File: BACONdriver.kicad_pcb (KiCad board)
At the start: 2 copper layers, 20 parts, among them P1 Batt_Mon, P10 Motor_Ctrl, P11 Batt, P4 Stearing, P5 D8, P6 V_Sel, P7 A5, P8 Batt_Current, P9 FTDI, U1 LM358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

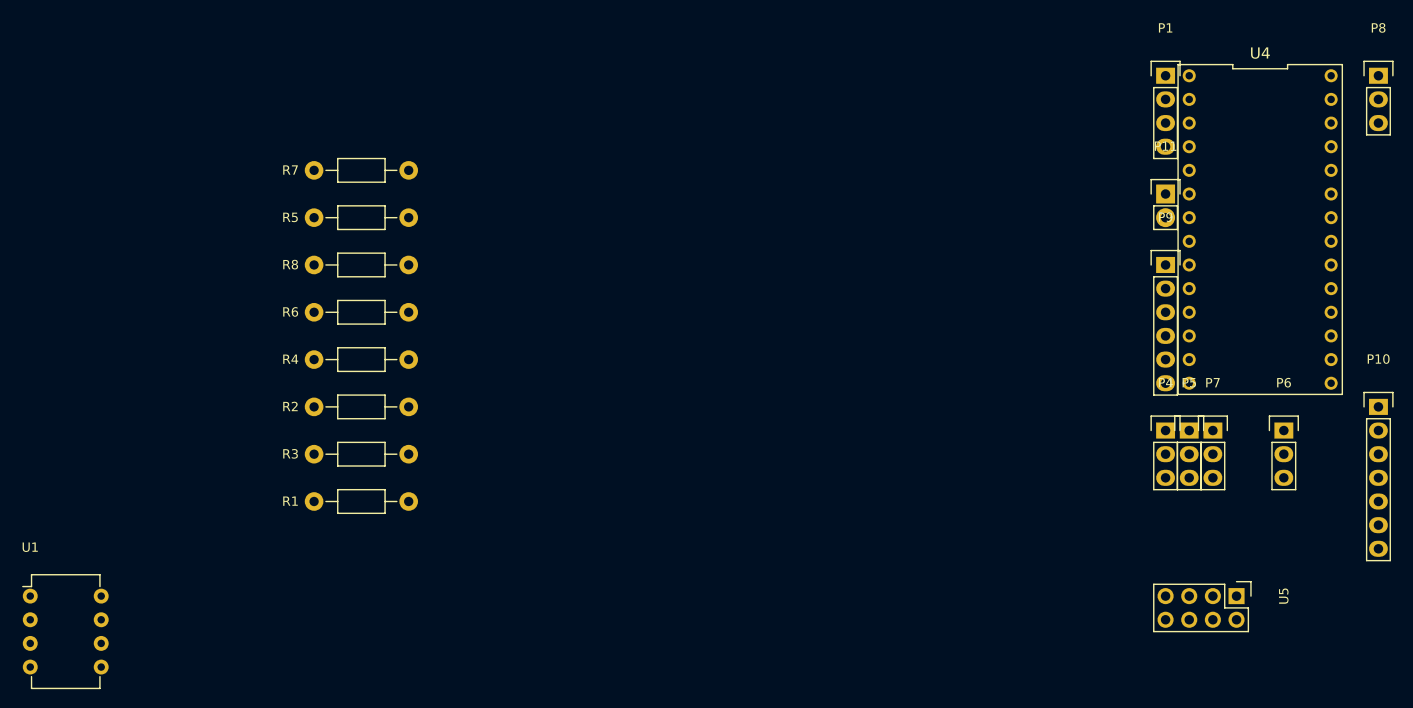
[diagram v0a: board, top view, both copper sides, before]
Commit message: Modified to use a simple voltage divider for battery voltage measurement, the op amp version would not fit on the prototype board and not really needed. Also added headers to allow the FTDI TX/RX to be swapped.
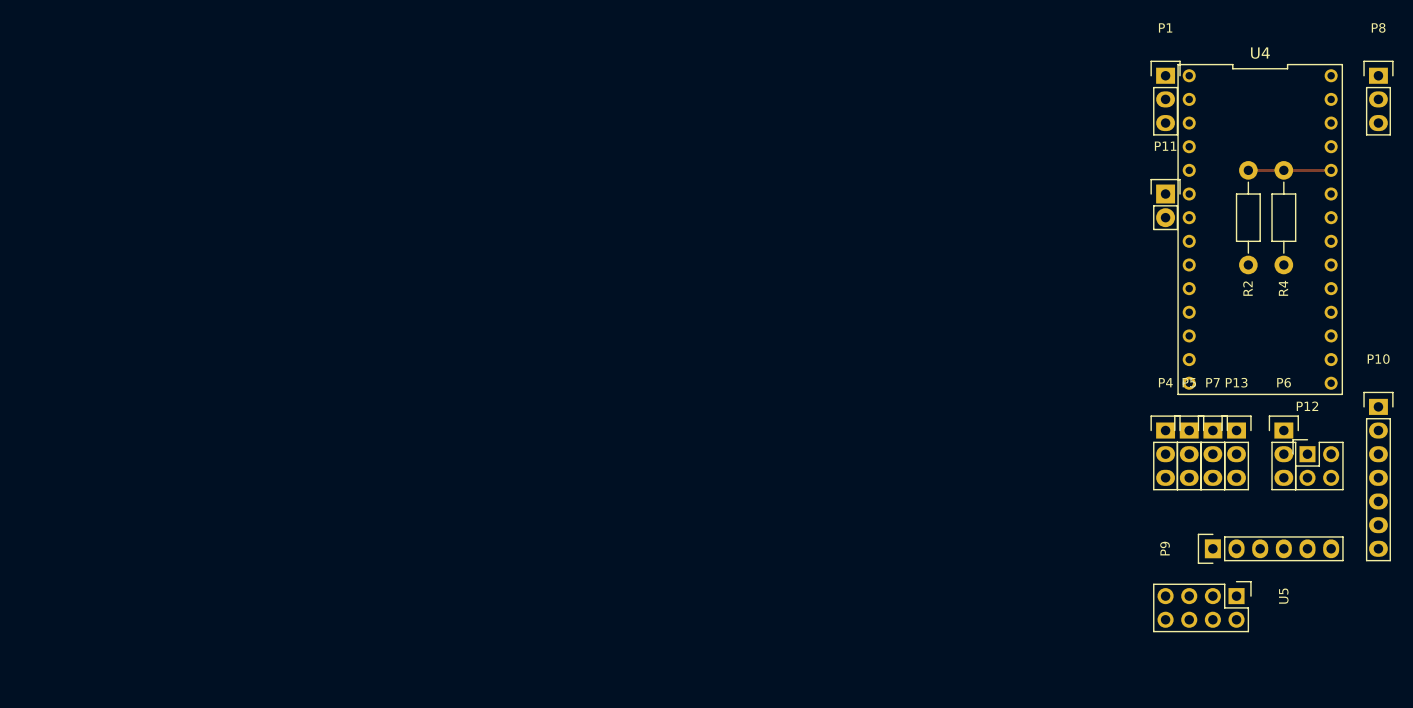
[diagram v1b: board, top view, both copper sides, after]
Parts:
- removed R1, R3, R5, R6, R7, R8: 10K, Resistors_ThroughHole:Resistor_Horizontal_RM10mm
- removed U1: LM358, Housings_DIP:DIP-8_W7.62mm
- added P12: Cross, Pin_Headers:Pin_Header_Straight_2x02, F.Cu at (172.7, 109.2)
- added P13: A5, Pin_Headers:Pin_Header_Straight_1x03, F.Cu at (165.1, 106.7)
- P1: footprint Pin_Headers:Pin_Header_Straight_1x04 -> Pin_Headers:Pin_Header_Straight_1x03
- P7: value A5 -> A4
- moved R4 104.6 mm to (170.2, 88.9), turned to 90 degrees
- moved R2 93.7 mm to (166.4, 78.7), turned to 270 degrees
- moved P9 30.9 mm to (162.6, 119.4), turned to 90 degrees
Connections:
- P7 pad 3: /Control_Board/A5 -> /Control_Board/A4
- P9 pad 4: /Control_Board/TXD -> Net-(P12-Pad3)
- P9 pad 5: /Control_Board/RXD -> Net-(P12-Pad2)
- R2 pad 1: Net-(R2-Pad1) -> /Control_Board/A1
- R2 pad 2: /Control_Board/A0 -> /Control_Board/Cell2
- R4 pad 2: Net-(R2-Pad1) -> /Control_Board/A1
- U4 pad 10: (no net) -> /Control_Board/A1
- U4 pad 4: (no net) -> /Control_Board/A4
- U4 pad 6: /Control_Board/CS_VAL -> (no net)
- U4 pad 8: /Control_Board/A2 -> /Control_Board/CS_VAL
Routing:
- net /Control_Board/A1: track 0.00 -> 8.89 mm
